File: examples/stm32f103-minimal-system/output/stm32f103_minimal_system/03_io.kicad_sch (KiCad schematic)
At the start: 3 parts, among them J2 SWD-4P

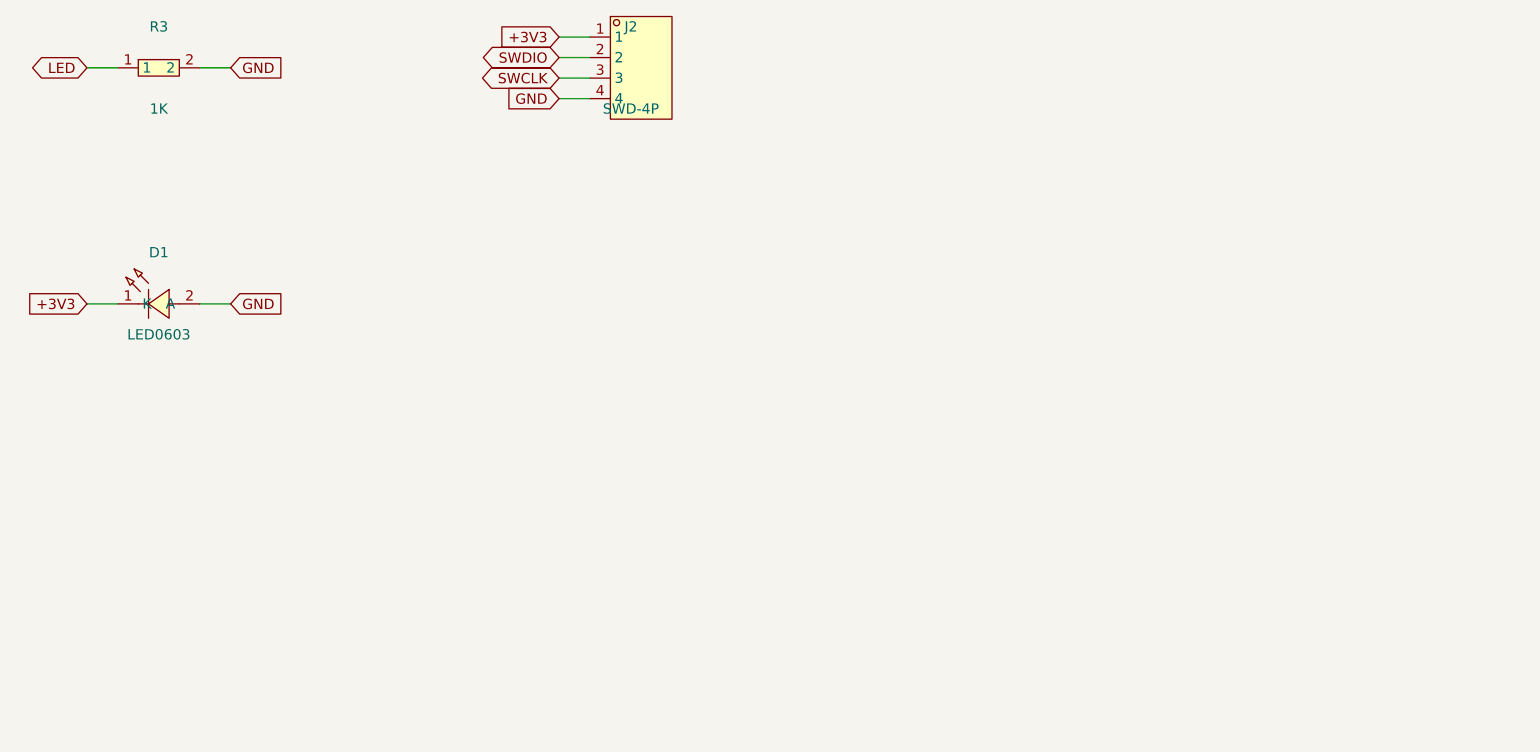
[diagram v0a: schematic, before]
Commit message: chore(example): update STM32F103 with easyeda2kicad symbols, footprints, and PCB layout 更新示例：easyeda2kicad 符号+封装、PCB 布局
- All symbols regenerated via easyeda2kicad (correct pin alignment)
- All footprints now have real pads from EasyEDA data
- Add pcb_layout.regions to circuit-model.json for agent-driven PCB placement
- Refresh schematics, reports, and operation logs from latest pipeline

Co-Authored-By: Claude Opus 4.7 <noreply@anthropic.com>
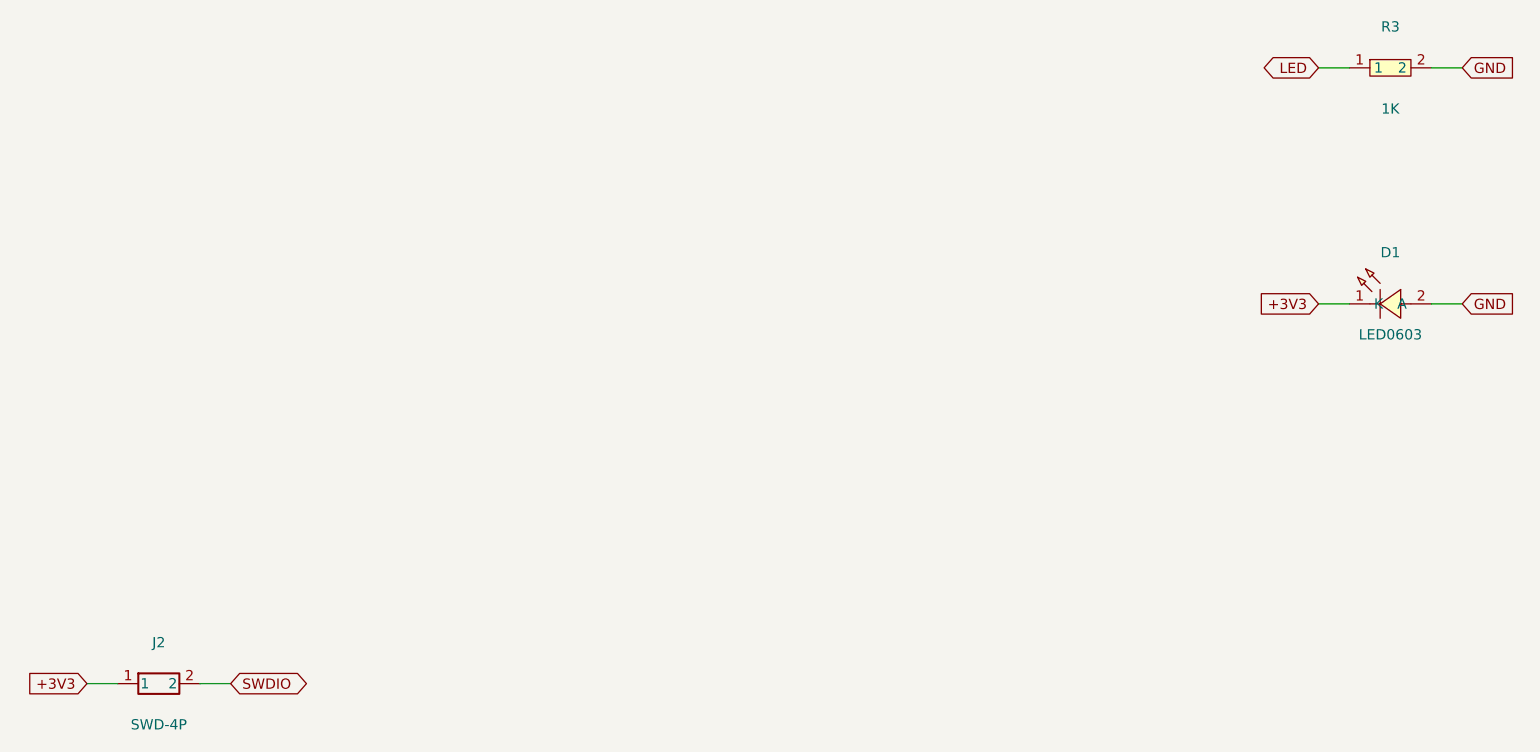
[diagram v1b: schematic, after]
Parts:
- removed J2: SWD-4P, symbol JLC-MCP:Header-Male-2.54_1x4
- added J2: SWD-4P, symbol JLC-MCP:2.54mm_1_2P
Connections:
- net +3V3: now also J2.1
- net SWDIO: now also J2.2
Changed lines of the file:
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@@
   (symbol
     (lib_id "JLC-MCP:RC0603JR-071KL")
-    (at 50.8 50.8 0)
+    (at 203.2 50.8 0)
     (unit 1)
     (exclude_from_sim no)
@@
     (on_board yes)
     (dnp no)
-    (property "Reference" "R3" (at 50.8 45.72 0)
+    (property "Reference" "R3" (at 203.2 45.72 0)
       (effects (font (size 1.27 1.27)))
     )
-    (property "Value" "1K" (at 50.8 55.88 0)
+    (property "Value" "1K" (at 203.2 55.88 0)
       (effects (font (size 1.27 1.27)))
     )
-    (property "Footprint" "" (at 50.8 50.8 0)
+    (property "Footprint" "" (at 203.2 50.8 0)
       (hide yes)
       (effects (font (size 1.27 1.27)))
@@
     (instances
       (project "stm32f103_minimal_system"
-        (path "/2d1f0816-bd2b-4906-9805-f249bd7cb4d6"
+        (path "/51849b38-550f-43b2-a05c-a3c441b16fd7"
           (reference "R3")
           (unit 1)
@@
   (symbol
     (lib_id "JLC-MCP:APHD1608LCGCK")
-    (at 50.8 78.74 0)
+    (at 203.2 78.74 0)
     (unit 1)
     (exclude_from_sim no)
@@
     (on_board yes)
     (dnp no)
-    (property "Reference" "D1" (at 50.8 73.66 0)
+    (property "Reference" "D1" (at 203.2 73.66 0)
       (effects (font (size 1.27 1.27)))
     )
-    (property "Value" "LED0603" (at 50.8 83.82 0)
+    (property "Value" "LED0603" (at 203.2 83.82 0)
       (effects (font (size 1.27 1.27)))
     )
-    (property "Footprint" "" (at 50.8 78.74 0)
+    (property "Footprint" "" (at 203.2 78.74 0)
       (hide yes)
       (effects (font (size 1.27 1.27)))
@@
     (instances
       (project "stm32f103_minimal_system"
-        (path "/2d1f0816-bd2b-4906-9805-f249bd7cb4d6"
+        (path "/51849b38-550f-43b2-a05c-a3c441b16fd7"
           (reference "D1")
           (unit 1)
@@
   )
   (symbol
-    (lib_id "JLC-MCP:Header-Male-2.54_1x4")
-    (at 109.22 50.8 0)
+    (lib_id "JLC-MCP:2.54mm_1_2P")
+    (at 50.8 127 0)
     (unit 1)
     (exclude_from_sim no)
@@
     (on_board yes)
     (dnp no)
-    (property "Reference" "J2" (at 109.22 45.72 0)
+    (property "Reference" "J2" (at 50.8 121.92 0)
       (effects (font (size 1.27 1.27)))
     )
-    (property "Value" "SWD-4P" (at 109.22 55.88 0)
+    (property "Value" "SWD-4P" (at 50.8 132.08 0)
       (effects (font (size 1.27 1.27)))
     )
-    (property "Footprint" "" (at 109.22 50.8 0)
+    (property "Footprint" "" (at 50.8 127 0)
       (hide yes)
       (effects (font (size 1.27 1.27)))
     )
-      (property "LCSC" "C124378" (at 0 0 0)
+      (property "LCSC" "C36717" (at 0 0 0)
         (hide yes)
         (effects (font (size 1.27 1.27)))
@@
     (instances
       (project "stm32f103_minimal_system"
-        (path "/2d1f0816-bd2b-4906-9805-f249bd7cb4d6"
+        (path "/51849b38-550f-43b2-a05c-a3c441b16fd7"
           (reference "J2")
           (unit 1)
@@
     )
   )
-  (wire (pts (xy 45.72 50.8) (xy 41.91 50.8))
+  (wire (pts (xy 198.12 50.8) (xy 194.31 50.8))
     (stroke (width 0) (type default))
   )
-  (global_label "LED" (shape bidirectional) (at 41.91 50.8 0)
+  (global_label "LED" (shape bidirectional) (at 194.31 50.8 0)
     (effects (font (size 1.27 1.27)) (justify right))
   )
-  (wire (pts (xy 55.88 50.8) (xy 59.69 50.8))
+  (wire (pts (xy 208.28 50.8) (xy 212.09 50.8))
     (stroke (width 0) (type default))
   )
-  (global_label "GND" (shape input) (at 59.69 50.8 0)
+  (global_label "GND" (shape input) (at 212.09 50.8 0)
     (effects (font (size 1.27 1.27)) (justify left))
   )
-  (wire (pts (xy 45.72 80.01) (xy 41.91 80.01))
+  (wire (pts (xy 198.12 80.01) (xy 194.31 80.01))
     (stroke (width 0) (type default))
   )
-  (global_label "+3V3" (shape input) (at 41.91 80.01 0)
+  (global_label "+3V3" (shape input) (at 194.31 80.01 0)
     (effects (font (size 1.27 1.27)) (justify right))
   )
-  (wire (pts (xy 55.88 80.01) (xy 59.69 80.01))
+  (wire (pts (xy 208.28 80.01) (xy 212.09 80.01))
     (stroke (width 0) (type default))
   )
-  (global_label "GND" (shape input) (at 59.69 80.01 0)
+  (global_label "GND" (shape input) (at 212.09 80.01 0)
     (effects (font (size 1.27 1.27)) (justify left))
   )
-  (wire (pts (xy 104.14 46.99) (xy 100.33 46.99))
+  (wire (pts (xy 45.72 127) (xy 41.91 127))
     (stroke (width 0) (type default))
   )
-  (global_label "+3V3" (shape input) (at 100.33 46.99 0)
+  (global_label "+3V3" (shape input) (at 41.91 127 0)
     (effects (font (size 1.27 1.27)) (justify right))
   )
-  (wire (pts (xy 104.14 49.53) (xy 100.33 49.53))
+  (wire (pts (xy 55.88 127) (xy 59.69 127))
     (stroke (width 0) (type default))
   )
-  (global_label "SWDIO" (shape bidirectional) (at 100.33 49.53 0)
-    (effects (font (size 1.27 1.27)) (justify right))
-  )
-  (wire (pts (xy 104.14 52.07) (xy 100.33 52.07))
-    (stroke (width 0) (type default))
-  )
-  (global_label "SWCLK" (shape bidirectional) (at 100.33 52.07 0)
-    (effects (font (size 1.27 1.27)) (justify right))
-  )
-  (wire (pts (xy 104.14 54.61) (xy 100.33 54.61))
-    (stroke (width 0) (type default))
-  )
-  (global_label "GND" (shape input) (at 100.33 54.61 0)
-    (effects (font (size 1.27 1.27)) (justify right))
+  (global_label "SWDIO" (shape bidirectional) (at 59.69 127 0)
+    (effects (font (size 1.27 1.27)) (justify left))
   )
   (sheet_instances
     (path "/" (page "1"))
-    (path "/44ec2dac-9deb-49fd-b388-f7e5c4aae55e" (page "2"))
-    (path "/9bbf9f8b-0e03-41fe-bf7d-9a9f96ccd11d" (page "3"))
-    (path "/2d1f0816-bd2b-4906-9805-f249bd7cb4d6" (page "4"))
+    (path "/1f9992b5-23c7-4baf-801a-52bbd93a87d8" (page "2"))
+    (path "/ec933af1-dbe3-44fd-835c-e9fede052fb8" (page "3"))
+    (path "/51849b38-550f-43b2-a05c-a3c441b16fd7" (page "4"))
   )
 )
